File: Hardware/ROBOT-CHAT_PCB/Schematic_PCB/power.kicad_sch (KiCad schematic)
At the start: 16 parts, among them J5 Conn_01x02, J6 Conn_01x02

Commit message: current schematic
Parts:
- BU33SD5WG-TR1: footprint BU33SD5WG-TR:BU33SD5WG-TR -> Package_TO_SOT_SMD:SOT-23-5
- C1, C19, C2, C20, C22, C23: footprint (none) -> Capacitor_SMD:C_0603_1608Metric
- J5, J6: footprint (none) -> Connector_JST:JST_PH_B2B-PH-K_1x02_P2.00mm_Vertical
- L3: footprint (none) -> Bobine_74404054068:Bobine_74404054068
- R1, R2, R7, R8, R9: footprint (none) -> Resistor_SMD:R_0603_1608Metric
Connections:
- net EN3.3 is gone; now on net +5V: BU33SD5WG-TR1.3 (STBY)
- net EN5 is gone; now on net +5V: MP1475DJ-LF-P1.6 (EN)
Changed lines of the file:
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@@
 	(wire
 		(pts
-			(xy 133.35 46.99) (xy 134.62 46.99)
+			(xy 133.35 46.99) (xy 137.16 46.99)
 		)
 		(stroke
@@
 		)
 	)
-	(hierarchical_label "EN5"
-		(shape input)
-		(at 215.9 39.37 180)
-		(effects
-			(font
-				(size 1.27 1.27)
-			)
-			(justify right)
-		)
-	)
-	(hierarchical_label "EN3.3"
-		(shape input)
-		(at 134.62 46.99 0)
-		(effects
-			(font
-				(size 1.27 1.27)
-			)
-			(justify left)
-		)
-	)
 	(symbol
 		(lib_id "power:GND")
@@
 			)
 		)
-		(property "Footprint" ""
+		(property "Footprint" "Resistor_SMD:R_0603_1608Metric"
 			(at 247.65 50.8 0)
 			(effects
@@
 			)
 		)
-		(property "Footprint" ""
+		(property "Footprint" "Connector_JST:JST_PH_B2B-PH-K_1x02_P2.00mm_Vertical"
 			(at 62.23 138.43 0)
 			(effects
@@
 			)
 		)
-		(property "Footprint" ""
+		(property "Footprint" "Resistor_SMD:R_0603_1608Metric"
 			(at 208.28 45.72 0)
 			(effects
@@
 			)
 		)
-		(property "Footprint" ""
+		(property "Footprint" "Resistor_SMD:R_0603_1608Metric"
 			(at 257.81 43.18 0)
 			(effects
@@
 			)
 		)
-		(property "Footprint" ""
+		(property "Footprint" "Connector_JST:JST_PH_B2B-PH-K_1x02_P2.00mm_Vertical"
 			(at 93.98 138.43 0)
 			(effects
@@
 			)
 		)
-		(property "Footprint" ""
+		(property "Footprint" "Capacitor_SMD:C_0603_1608Metric"
 			(at 201.93 53.34 0)
 			(effects
@@
 			)
 		)
-		(property "Footprint" ""
+		(property "Footprint" "Capacitor_SMD:C_0603_1608Metric"
 			(at 95.25 48.26 0)
 			(effects
@@
 			)
 		)
-		(property "Footprint" ""
+		(property "Footprint" "Capacitor_SMD:C_0603_1608Metric"
 			(at 144.78 44.45 0)
 			(effects
@@
 			)
 		)
-		(property "Footprint" "BU33SD5WG-TR:BU33SD5WG-TR"
+		(property "Footprint" "Package_TO_SOT_SMD:SOT-23-5"
 			(at 122.174 25.654 0)
 			(effects
@@
 			)
 		)
-		(property "Footprint" ""
+		(property "Footprint" "Capacitor_SMD:C_0603_1608Metric"
 			(at 204.47 30.48 0)
 			(effects
@@
 			)
 		)
-		(property "Footprint" ""
+		(property "Footprint" "Bobine_74404054068:Bobine_74404054068"
 			(at 248.92 40.64 0)
 			(effects
@@
 			)
 		)
-		(property "Footprint" ""
+		(property "Footprint" "Capacitor_SMD:C_0603_1608Metric"
 			(at 243.84 35.56 0)
 			(effects
@@
 	)
 	(symbol
+		(lib_id "power:+5V")
+		(at 137.16 46.99 270)
+		(unit 1)
+		(exclude_from_sim no)
+		(in_bom yes)
+		(on_board yes)
+		(dnp no)
+		(property "Reference" "#PWR0301"
+			(at 133.35 46.99 0)
+			(effects
+				(font
+					(size 1.27 1.27)
+				)
+				(hide yes)
+			)
+		)
+		(property "Value" "+5V"
+			(at 137.668 48.768 90)
+			(effects
+				(font
+					(size 1.27 1.27)
+				)
+				(justify left)
+			)
+		)
+		(property "Footprint" ""
+			(at 137.16 46.99 0)
+			(effects
+				(font
+					(size 1.27 1.27)
+				)
+				(hide yes)
+			)
+		)
+		(property "Datasheet" ""
+			(at 137.16 46.99 0)
+			(effects
+				(font
+					(size 1.27 1.27)
+				)
+				(hide yes)
+			)
+		)
+		(property "Description" "Power symbol creates a global label with name \"+5V\""
+			(at 137.16 46.99 0)
+			(effects
+				(font
+					(size 1.27 1.27)
+				)
+				(hide yes)
+			)
+		)
+		(pin "1"
+		)
+		(instances
+			(project ""
+				(path "/3534a4da-1897-4a3c-809d-843e7f41fadb/9eede499-7e43-406d-a40f-aa5717e0debc"
+					(reference "#PWR0301")
+					(unit 1)
+				)
+			)
+		)
+	)
+	(symbol
 		(lib_id "Device:R_Small")
 		(at 242.57 45.72 90)
@@
 			)
 		)
-		(property "Footprint" ""
+		(property "Footprint" "Resistor_SMD:R_0603_1608Metric"
 			(at 242.57 45.72 0)
 			(effects
@@
 	)
 	(symbol
+		(lib_id "power:+5V")
+		(at 215.9 39.37 90)
+		(unit 1)
+		(exclude_from_sim no)
+		(in_bom yes)
+		(on_board yes)
+		(dnp no)
+		(property "Reference" "#PWR0302"
+			(at 219.71 39.37 0)
+			(effects
+				(font
+					(size 1.27 1.27)
+				)
+				(hide yes)
+			)
+		)
+		(property "Value" "+5V"
+			(at 213.36 37.846 90)
+			(effects
+				(font
+					(size 1.27 1.27)
+				)
+				(justify left)
+			)
+		)
+		(property "Footprint" ""
+			(at 215.9 39.37 0)
+			(effects
+				(font
+					(size 1.27 1.27)
+				)
+				(hide yes)
+			)
+		)
+		(property "Datasheet" ""
+			(at 215.9 39.37 0)
+			(effects
+				(font
+					(size 1.27 1.27)
+				)
+				(hide yes)
+			)
+		)
+		(property "Description" "Power symbol creates a global label with name \"+5V\""
+			(at 215.9 39.37 0)
+			(effects
+				(font
+					(size 1.27 1.27)
+				)
+				(hide yes)
+			)
+		)
+		(pin "1"
+		)
+		(instances
+			(project ""
+				(path "/3534a4da-1897-4a3c-809d-843e7f41fadb/9eede499-7e43-406d-a40f-aa5717e0debc"
+					(reference "#PWR0302")
+					(unit 1)
+				)
+			)
+		)
+	)
+	(symbol
 		(lib_id "Device:C_Small")
 		(at 257.81 34.29 0)
@@
 			)
 		)
-		(property "Footprint" ""
+		(property "Footprint" "Capacitor_SMD:C_0603_1608Metric"
 			(at 257.81 34.29 0)
 			(effects
@@
 			)
 		)
-		(property "Footprint" ""
+		(property "Footprint" "Resistor_SMD:R_0603_1608Metric"
 			(at 241.3 30.48 0)
 			(effects

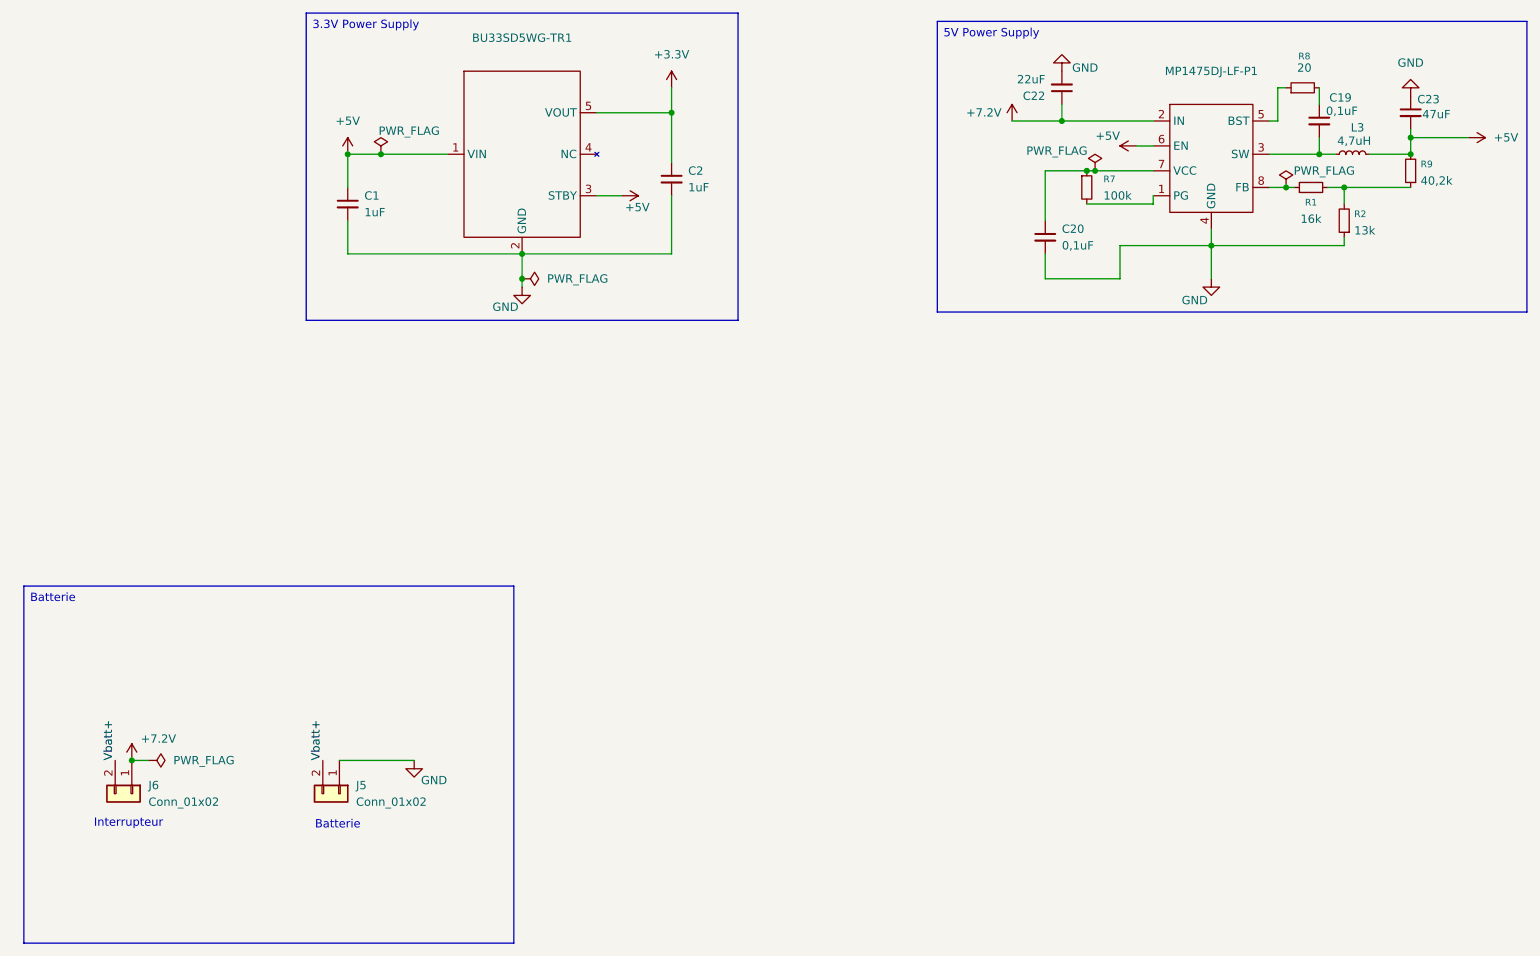
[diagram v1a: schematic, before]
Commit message: Rerouting avec Mr Fiack
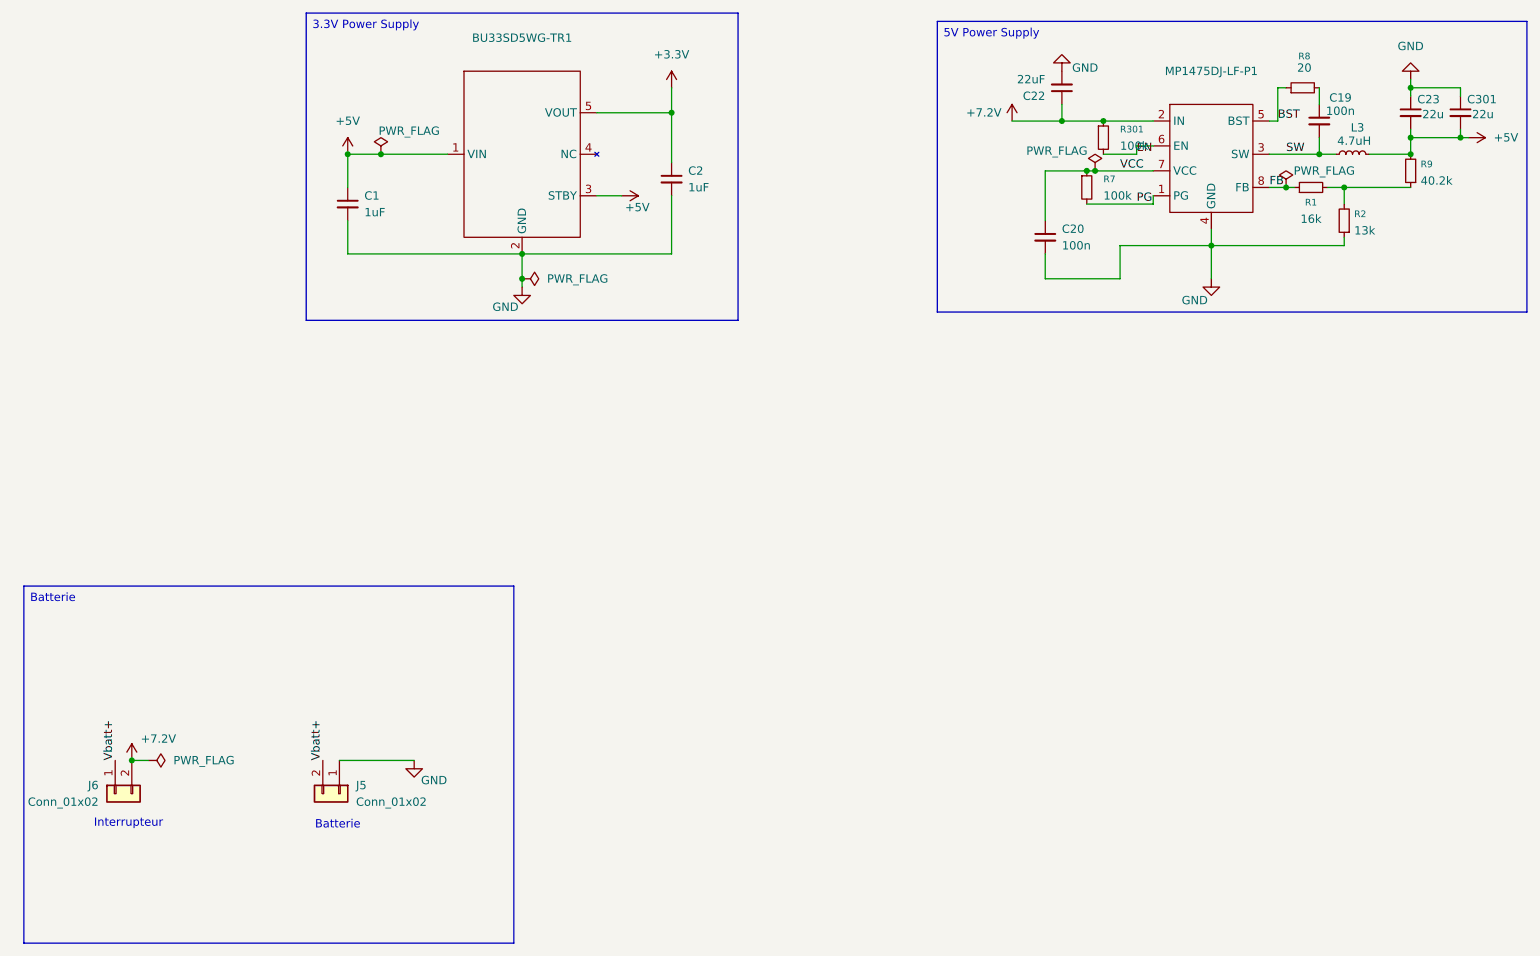
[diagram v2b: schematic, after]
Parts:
- added C301: 22u, Capacitor_SMD:C_0805_2012Metric, symbol Device:C_Small
- added R301: 100k, Resistor_SMD:R_0402_1005Metric, symbol Device:R_Small
- C19, C20: value 0,1uF -> 100n; footprint Capacitor_SMD:C_0603_1608Metric -> Capacitor_SMD:C_0402_1005Metric
- C22: footprint Capacitor_SMD:C_0603_1608Metric -> Capacitor_SMD:C_0805_2012Metric
- C23: value 47uF -> 22u; footprint Capacitor_SMD:C_0603_1608Metric -> Capacitor_SMD:C_0805_2012Metric
- L3: value 4,7uH -> 4.7uH
- R1, R2, R7, R8: footprint Resistor_SMD:R_0603_1608Metric -> Resistor_SMD:R_0402_1005Metric
- R9: value 40,2k -> 40.2k; footprint Resistor_SMD:R_0603_1608Metric -> Resistor_SMD:R_0402_1005Metric
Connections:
- net +5V: now also C301.2; no longer MP1475DJ-LF-P1.6 (EN)
- net +7.2V: now also J6.2 (Pin_2), R301.1; no longer J6.1 (Pin_1)
- net GND: now also C301.1
- net Vbatt+: now also J6.1 (Pin_1); no longer J6.2 (Pin_2)
- net PG: now reaches MP1475DJ-LF-P1.1 (PG), R7.2
- net SW: now reaches C19.2, L3.1, MP1475DJ-LF-P1.3 (SW)
- net BST: now reaches MP1475DJ-LF-P1.5 (BST), R8.1
- net VCC: now reaches C20.1, MP1475DJ-LF-P1.7 (VCC), R7.1
- net FB: now reaches MP1475DJ-LF-P1.8 (FB), R1.1
- new net EN: MP1475DJ-LF-P1.6 (EN), R301.2
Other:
- moved on the sheet: J6
